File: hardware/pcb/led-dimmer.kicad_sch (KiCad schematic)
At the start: 15 parts, among them Q2 DMP3013SFV, U1 MIC1555YM5-TR

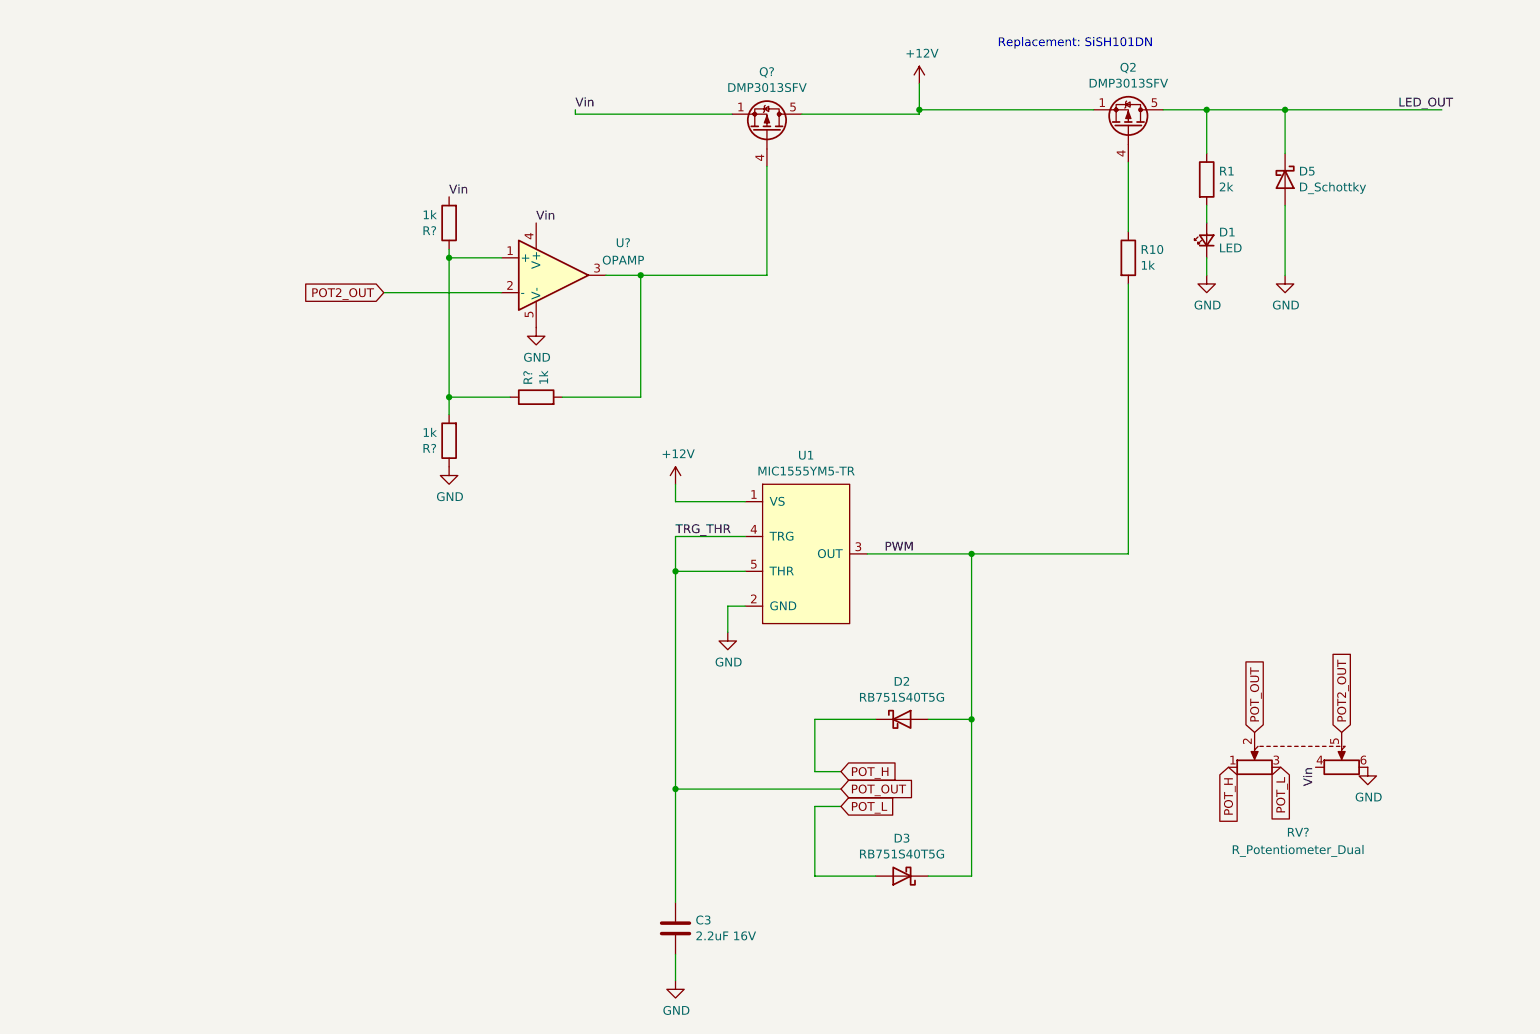
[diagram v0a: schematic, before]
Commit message: Schematic done
Made some of the footprint and layout.
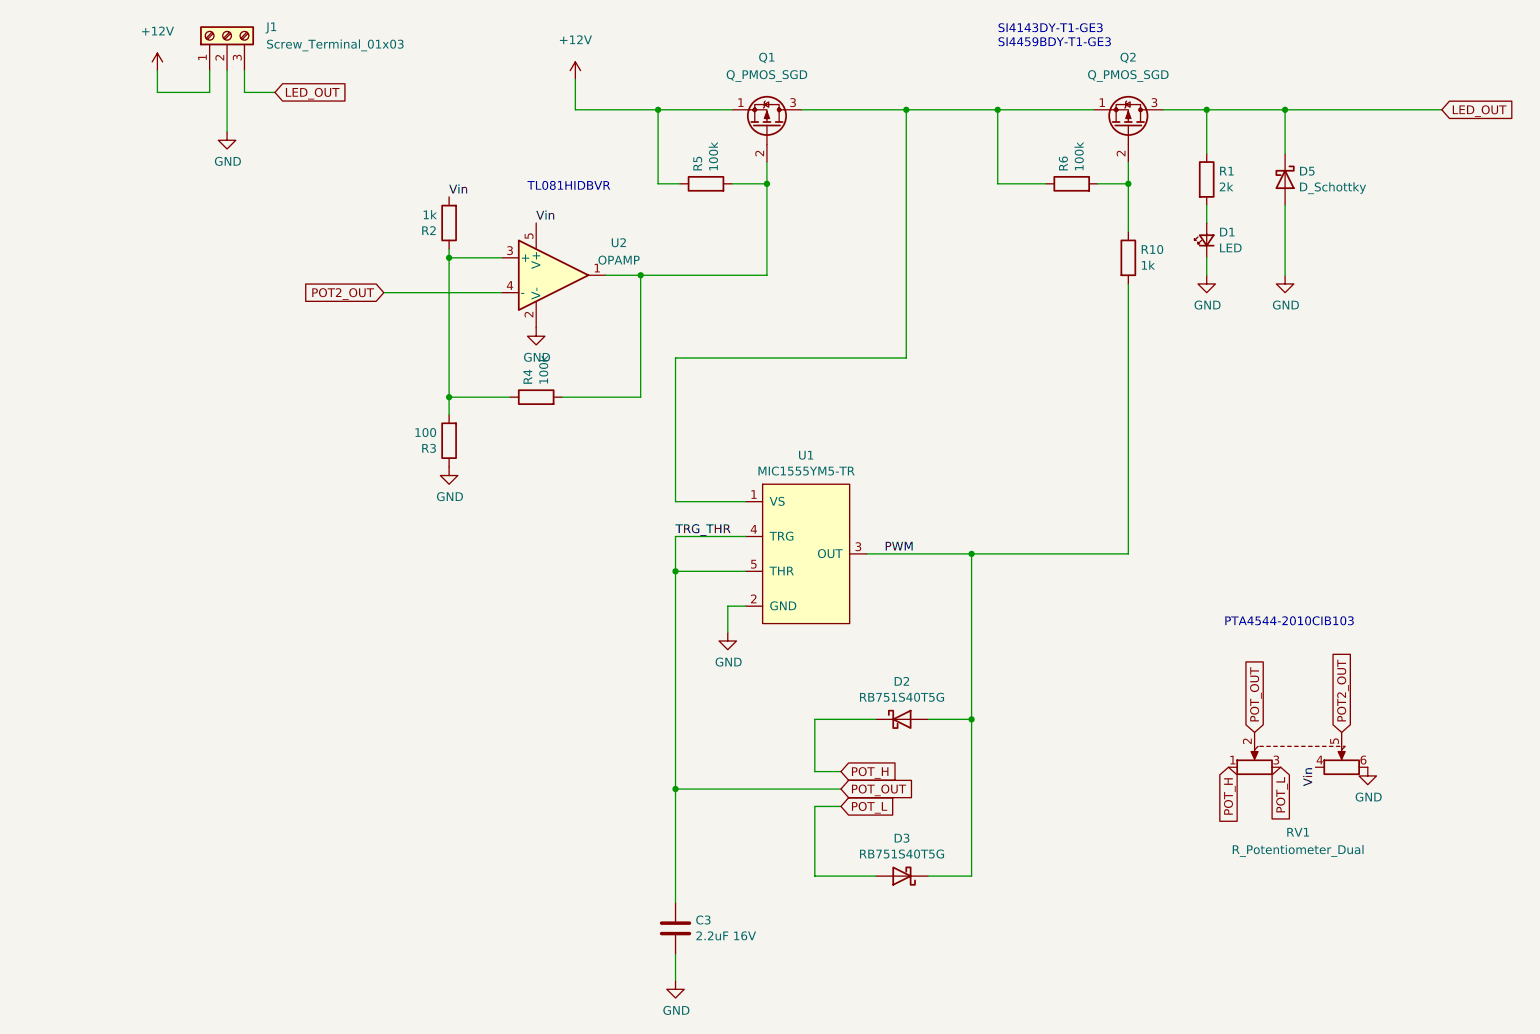
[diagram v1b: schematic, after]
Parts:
- removed Q2, Q?: DMP3013SFV, Package_SON:Diodes_PowerDI3333-8, symbol Transistor_FET:DMP3013SFV
- removed U?: OPAMP, symbol Simulation_SPICE:OPAMP
- added J1: Screw_Terminal_01x03, symbol Connector:Screw_Terminal_01x03
- added Q1, Q2: Q_PMOS_SGD, led_dimmer:SI4143DY-T1-GE3, symbol Device:Q_PMOS_SGD
- added R5, R6: 100k, Resistor_SMD:R_0603_1608Metric, symbol Device:R
- added U2: OPAMP, Package_TO_SOT_SMD:SOT-23-5, symbol led_dimmer:OPAMP
- R3: renamed from R?; value 1k -> 100
- R4: renamed from R?; value 1k -> 100k
- RV1: renamed from RV?; footprint (none) -> led_dimmer:PTA4544-2010CIB103
- gave numbers to parts that had none: 1
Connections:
- net +12V: now also J1.1 (Pin_1), Q1.1 (S), R5.1; no longer U1.1 (VS)
- net GND: now also J1.2 (Pin_2), U2.2 (V-)
- net LED_OUT: now also J1.3 (Pin_3), Q2.3 (D)
- net POT2_OUT: now also U2.4 (-)
- net Vin: now also U2.5 (V+)
- net at R10.1: now also Q2.2 (G), R6.2
- net at R2.1, R3.2, R4.1: now also U2.3 (+)
- net at R4.2: now also Q1.2 (G), R5.2, U2.1
- new net: Q1.3 (D), Q2.1 (S), R6.1, U1.1 (VS)
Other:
- note added: "PTA4544-2010CIB103"
- note added: "SI4143DY-T1-GE3 SI4459BDY-T1-GE3"
- note added: "TL081HIDBVR"
- note removed: "Replacement: SiSH101DN"

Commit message: First release
A first release which is ordered from JLC.
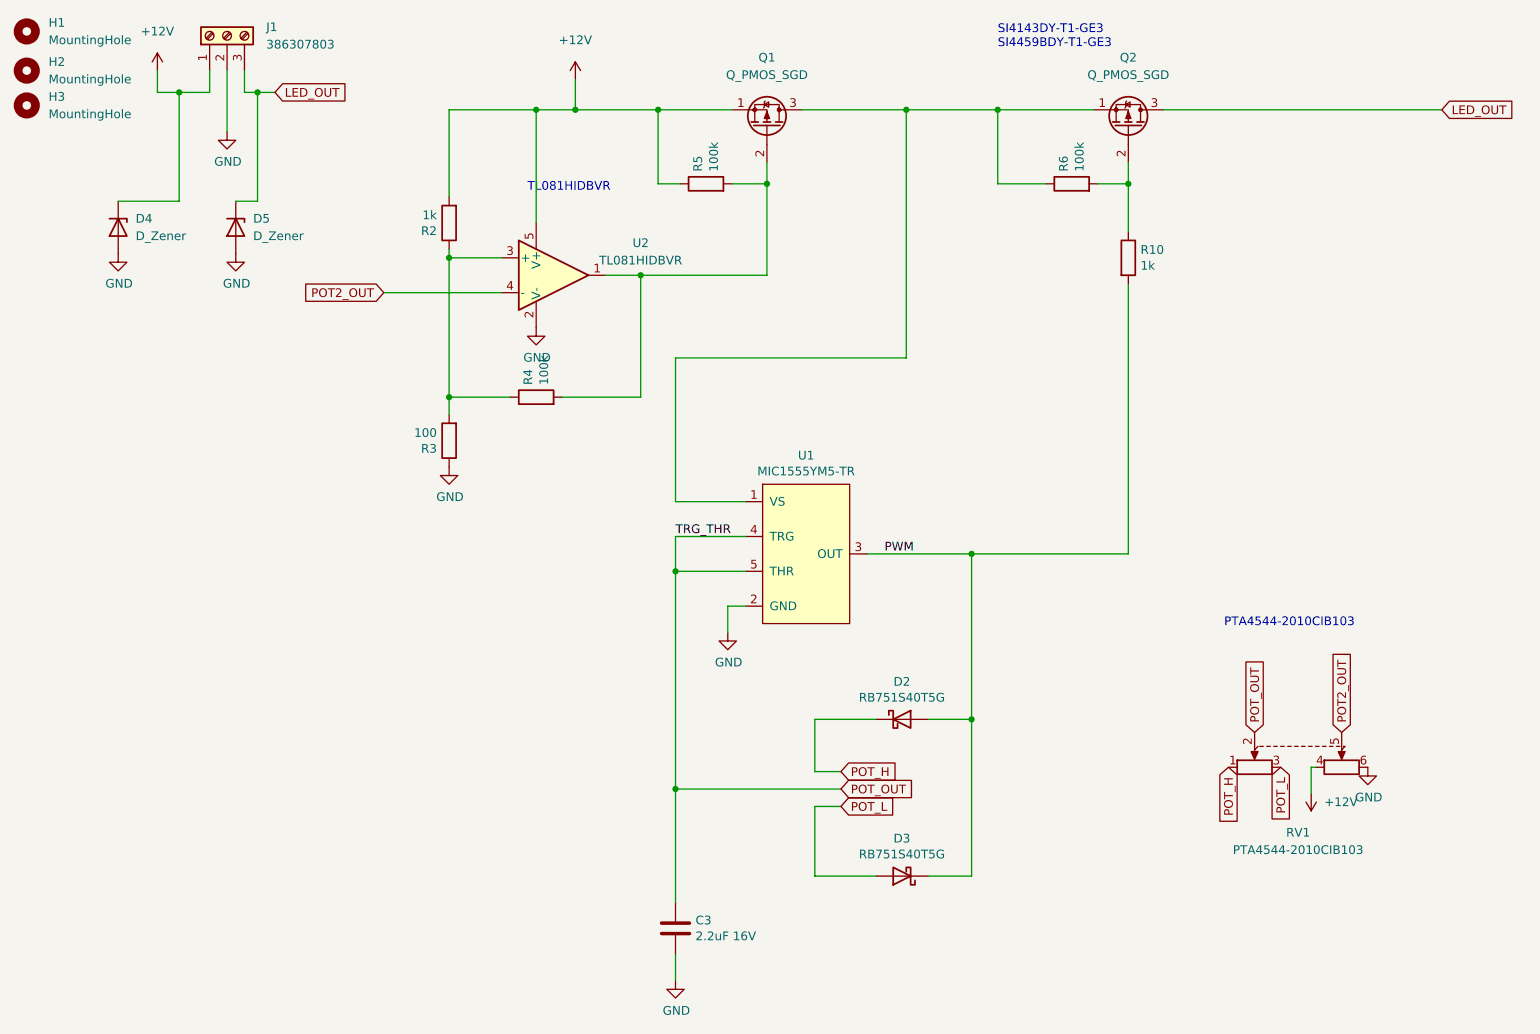
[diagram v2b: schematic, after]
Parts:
- removed D1: LED, LED_SMD:LED_0603_1608Metric, symbol Device:LED_Small
- removed D5: D_Schottky, Diode_SMD:D_SOD-123, symbol Device:D_Schottky
- removed R1: 2k, Resistor_SMD:R_0603_1608Metric, symbol Device:R
- added D4, D5: D_Zener, Diode_SMD:D_SOD-128, symbol Device:D_Zener
- added H1, H2, H3: MountingHole, MountingHole:MountingHole_3.2mm_M3_Pad_Via, symbol Mechanical:MountingHole
- J1: value Screw_Terminal_01x03 -> 386307803; footprint (none) -> led_dimmer:386307803
- RV1: value R_Potentiometer_Dual -> PTA4544-2010CIB103
- U2: value OPAMP -> TL081HIDBVR
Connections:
- net Vin is gone; now on net +12V: R2.2, RV1.4, U2.5 (V+)
- net +12V: now also D4.1 (K)
- net GND: now also D4.2 (A), D5.2 (A)
- net LED_OUT: now also D5.1 (K)
